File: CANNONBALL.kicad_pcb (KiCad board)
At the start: 4 copper layers, 25.6 x 23.6 mm, 66 parts, among them J3 JST-PH 2.0 BATTERY, J4 I2C_CONN, J5 LEFT_PINS, J6 RIGHT_PINS, Q1 FS8205A, Q2 DMG2301L, SW1 SW_Push, U1 USBLC6-4SC6, U10 MAX17048, U2 AP2112K-3.3, U3 ESP32-C3-WROOM-02, U4 LSM6DS3, U5 DW01A, U6 BQ24075RGT, U7 SHT40, U8 VEML6030

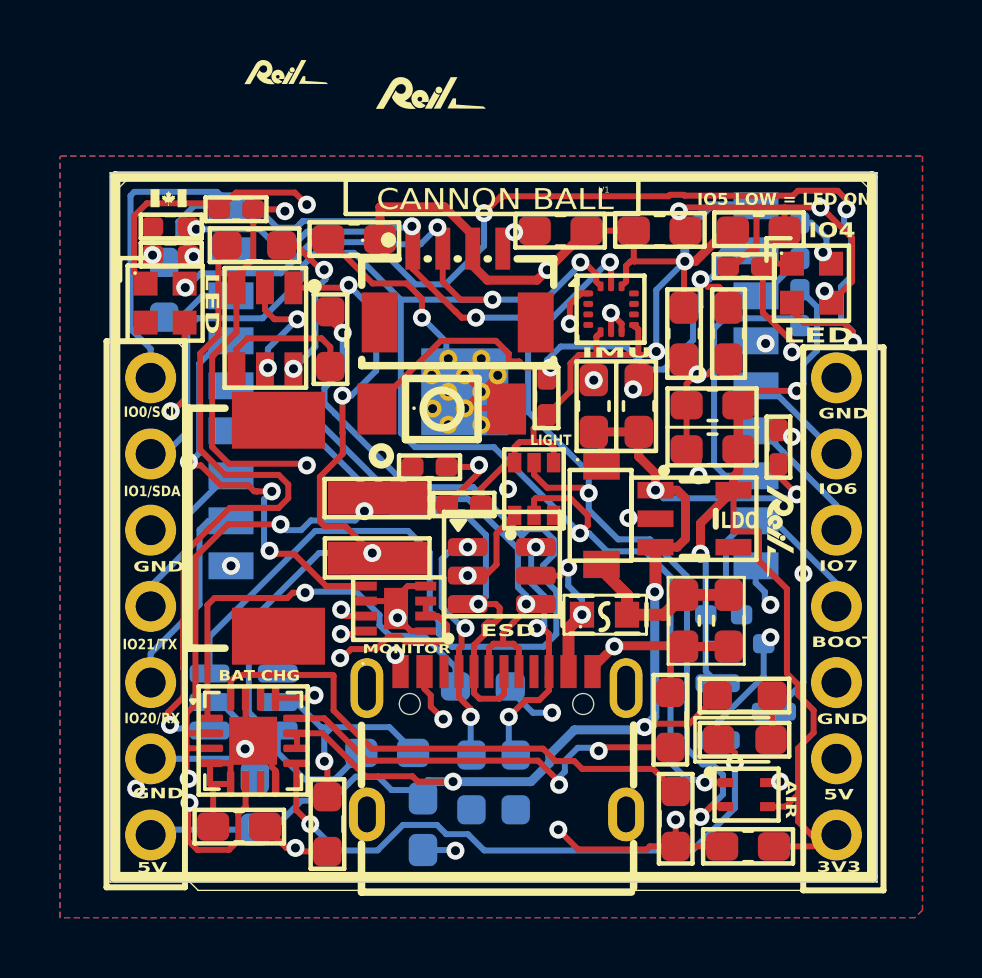
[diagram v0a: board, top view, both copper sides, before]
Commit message: Update silkscreen
Co-Authored-By: Claude Sonnet 4.6 <noreply@anthropic.com>
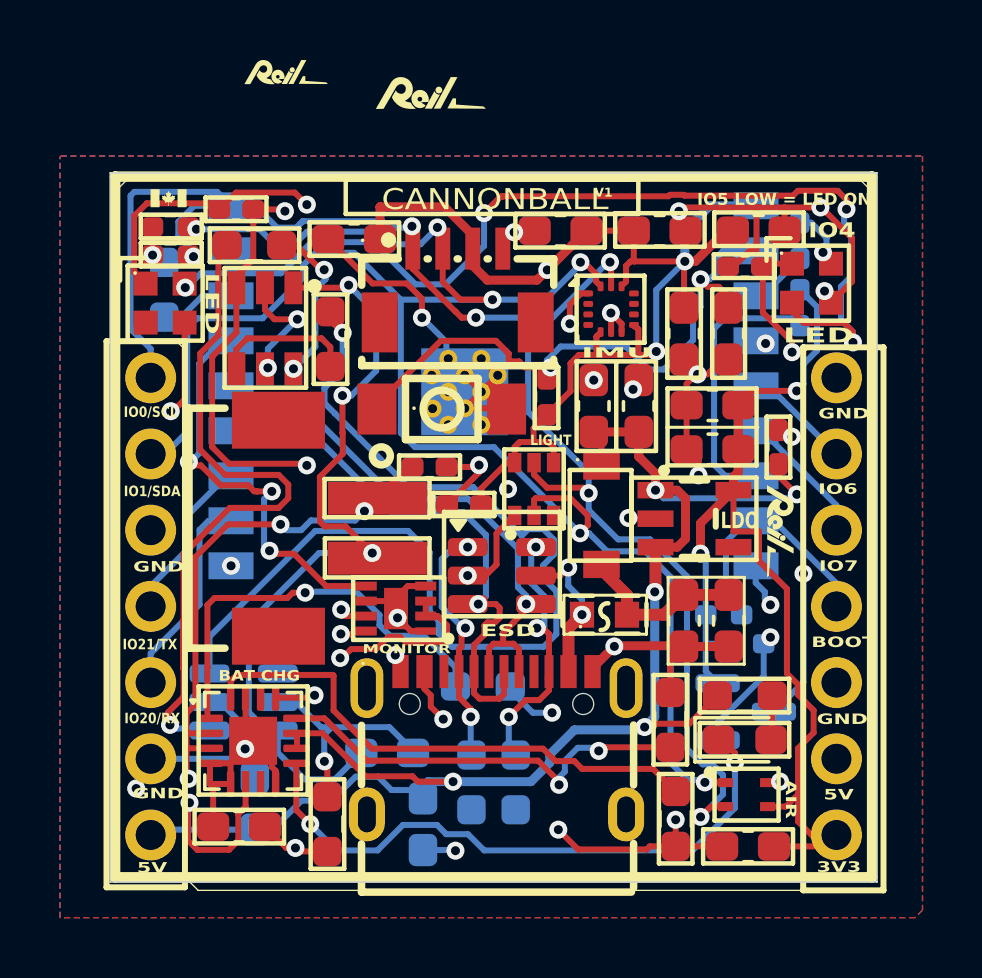
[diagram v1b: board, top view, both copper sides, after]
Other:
- board text added: "CANNONBALL"
- board text removed: "CANNON BALL"

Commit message: Fix silkscreen text sizes for JLC manufacturability
Updated all silkscreen text to 0.5x0.5mm with 0.1mm stroke, matching
previously verified board spec that passes JLC's process requirements.

Co-Authored-By: Claude Sonnet 4.6 <noreply@anthropic.com>
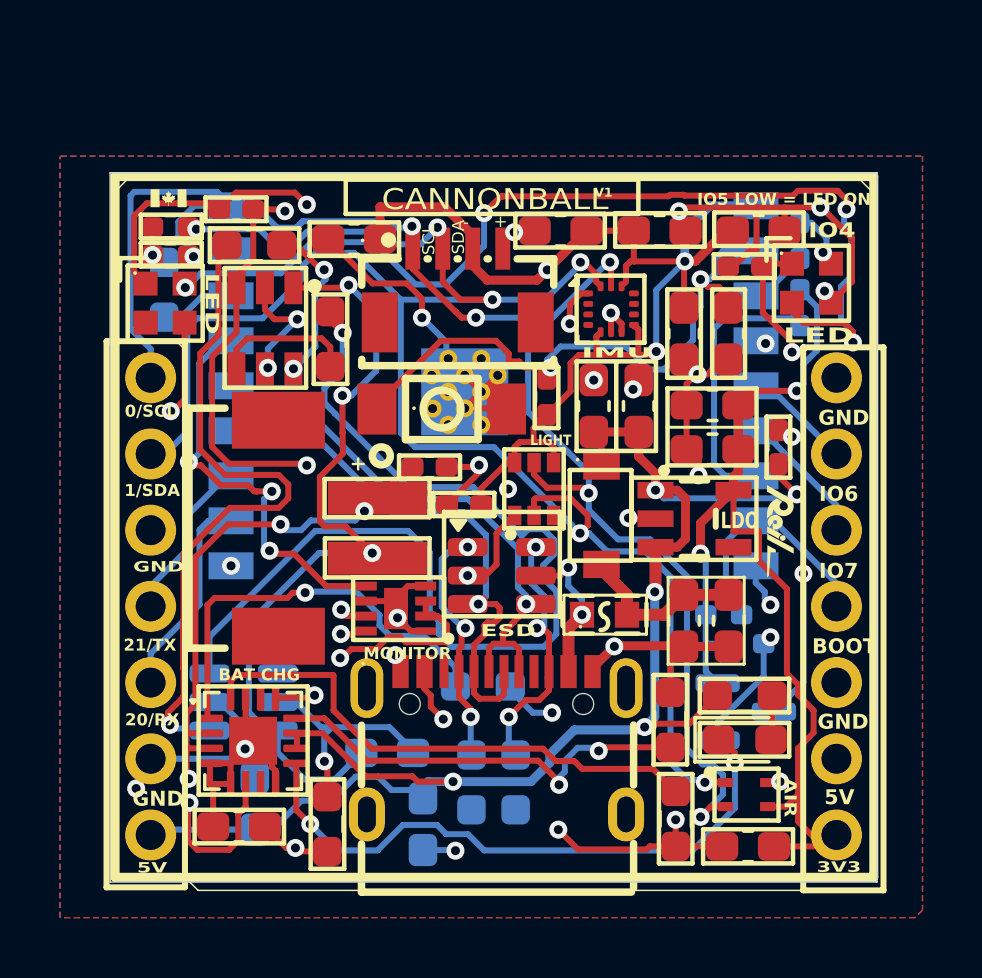
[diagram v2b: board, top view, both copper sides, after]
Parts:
- removed the G*** at (194.8, 101.0)
- removed the G*** at (190.0, 100.2)
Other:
- board text added: "+"
- board text added: "-"
- board text added: "0/SCL"
- board text added: "1/SDA"
- board text added: "20/RX"
- board text added: "21/TX"
- board text added: "SCL"
- board text added: "SDA"
- board text removed: "IO0/SCL"
- board text removed: "IO1/SDA"
- board text removed: "IO20/RX"
- board text removed: "IO21/TX"

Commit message: Add production_files to gitignore and update design files
Co-Authored-By: Claude Sonnet 4.6 <noreply@anthropic.com>
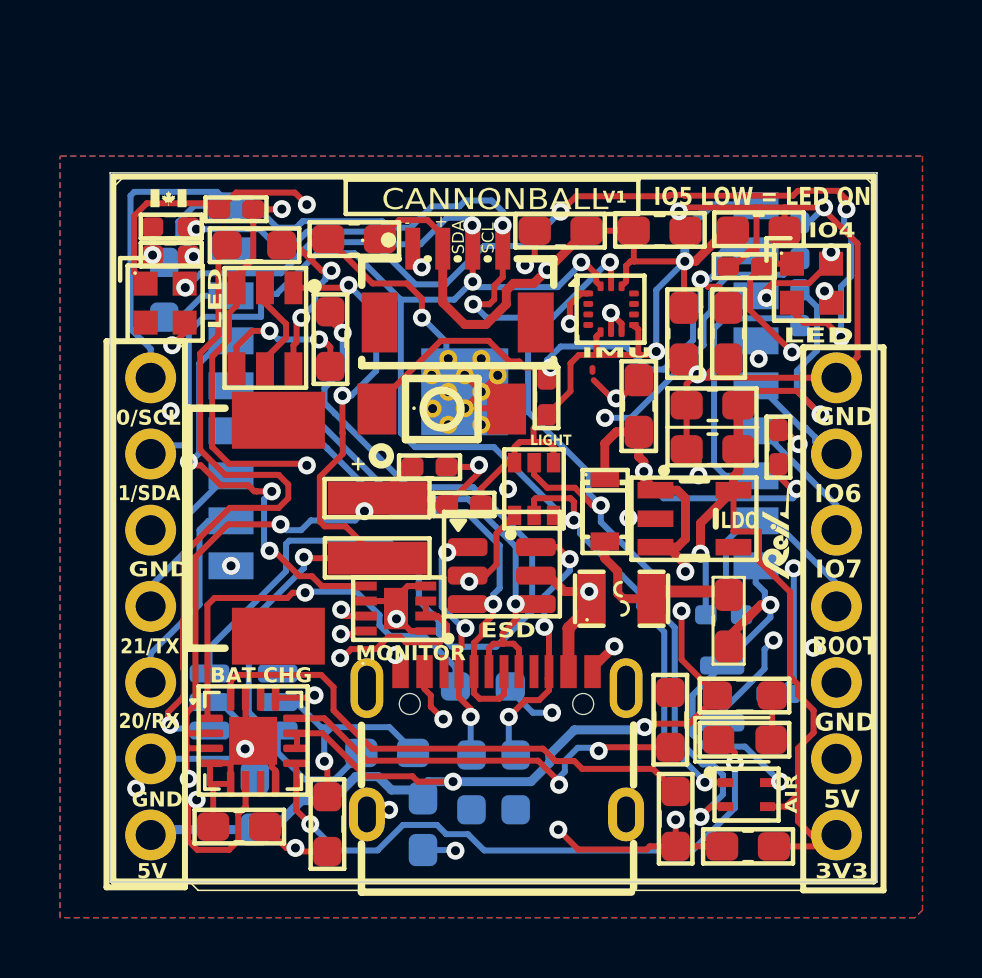
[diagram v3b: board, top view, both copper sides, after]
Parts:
- removed C2, C7: 100nF, Capacitor_SMD:C_0603_1608Metric_Pad1.08x0.95mm_HandSolder
- removed D1: 1N5819W, diode:SOD-123_L2.7-W1.6-LS3.7-RD
- removed F1: MF-FSMF050X-2, power:F0603
- removed Q2: DMG2301L, Package_TO_SOT_SMD:SOT-23
- removed R9: 10K, Resistor_SMD:R_0402_1005Metric_Pad0.72x0.64mm_HandSolder
- added D2: MS2A40LWS, diode:SOD-323_L1.7-W1.25-LS2.5-RD, F.Cu at (200.6, 114.8)
- added F2: 0805L110/16WR, power:F0805, F.Cu at (201.1, 117.7)
- added Q3: 2N7002K, Package_TO_SOT_SMD:SOT-23, B.Cu at (205.4, 120.9)
- C1: value 10uF -> 1uF
- C10, C11, C14, C16, C18, C19, C20, C21, C22, C23, C24, C3: value 100nF -> 1uF
- C15, C6: value 10uF -> 4.7uF
- R8: value 330 -> 10K
- U6: value BQ24075RGT -> TI BQ24075RGTR
- moved G*** 0.57 mm to (203.8, 124.5)
- turned G*** to 90 degrees
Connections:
- C19 pad 2: LED_3V3 -> 5V
- C23 pad 2: LED_3V3 -> 5V
- J4 pad 1: GPIO 0 / SCL -> GND
- J4 pad 2: GPIO 1 / SDA -> 3V3
- J4 pad 3: 3V3 -> GPIO 1 / SDA
- J4 pad 4: GND -> GPIO 0 / SCL
- LED1 pad 1: LED_3V3 -> 5V
- LED1 pad 3: GND -> LED_GND
- LED1 pad 4: Net-(LED1-DIN) -> GPIO 4
- LED2 pad 1: LED_3V3 -> 5V
- LED2 pad 3: GND -> LED_GND
- R8 pad 1: Net-(LED1-DIN) -> GND
- R8 pad 2: GPIO 4 -> GPIO 5
- USB1 pad 13: unconnected-(USB1-EH-Pad13)_1 -> GND
- USB1 pad 14: unconnected-(USB1-EH-Pad14) -> GND
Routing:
- net LED_3V3: track 44.9 -> 0.00 mm, vias 3 -> 0
- net LED_GND: track 0.00 -> 44.8 mm, vias 0 -> 3
- net 5V: track 65.4 -> 103.0 mm, vias 6 -> 9
- net GND: track 117.3 -> 142.7 mm, vias 29 -> 30
- net GPIO 5: track 14.7 -> 29.1 mm, vias 2 -> 3
- net GPIO 0 / SCL: track 64.9 -> 69.4 mm
- net G_CHARGE: track 34.1 -> 30.9 mm
- net Net-(LED1-DIN): track 2.10 -> 0.00 mm, vias 1 -> 0
- net Net-(LED1-DOUT): track 33.7 -> 32.1 mm
- net GPIO 4: track 1.68 -> 3.19 mm, vias 0 -> 2
- net GPIO 1 / SDA: track 73.5 -> 72.4 mm
- net 3V3: track 120.0 -> 121.0 mm
- net B+: track 37.3 -> 38.2 mm
- net VBUS: track 13.3 -> 14.1 mm, vias 3 -> 2
- net CC1: track 8.38 -> 7.65 mm
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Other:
- board text added: "07/26"
